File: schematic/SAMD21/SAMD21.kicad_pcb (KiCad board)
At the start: 4 copper layers, 100 x 100 mm, 54 parts, among them IC1 ATSAMD21G18A-AU, IC2 AZ1117IH-3.3TRG1, IC3 MCP2221-I_SL, J1 Barrel_Jack_Switch, J10 Conn_02x06_Odd_Even, J11 Conn_02x06_Odd_Even, J12 Conn_02x06_Odd_Even, J13 Conn_01x02, J14 Conn_02x05_Odd_Even, J15 Conn_01x08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

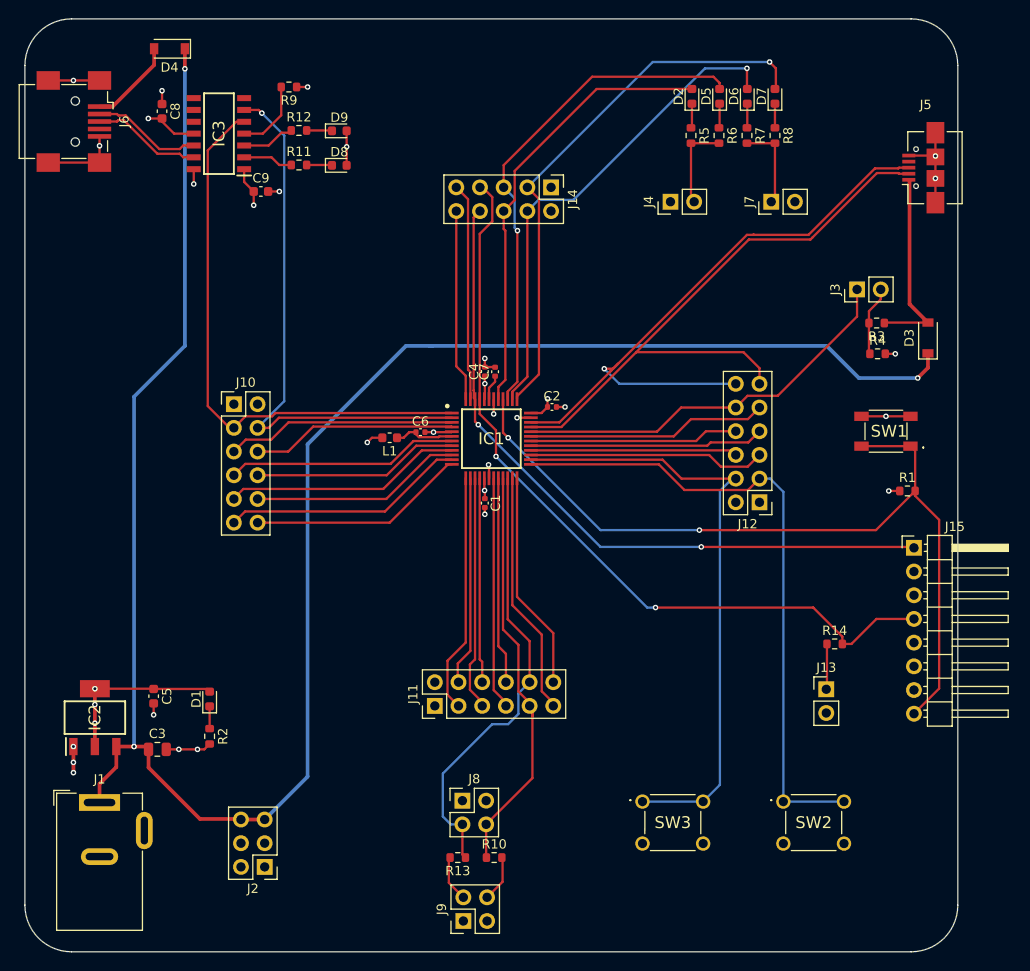
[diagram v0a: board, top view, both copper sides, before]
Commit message: Minor trace adjustments and some labels
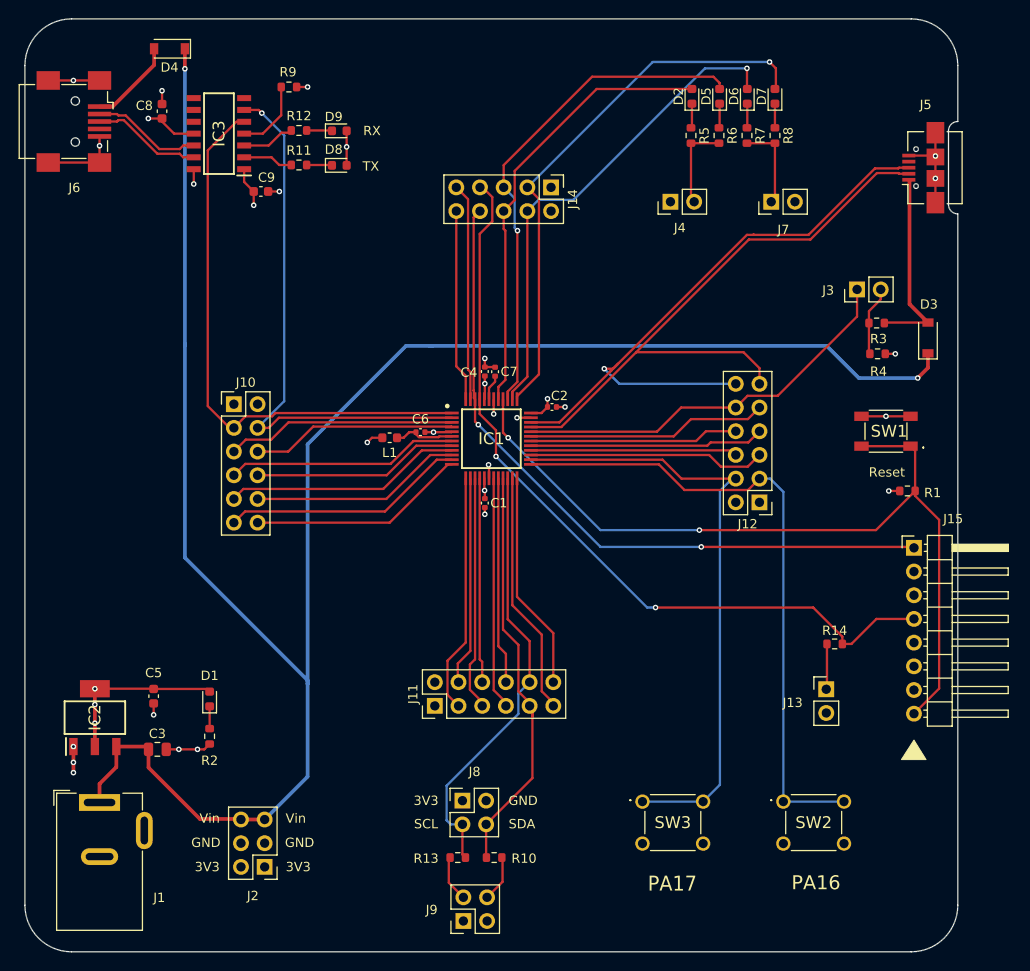
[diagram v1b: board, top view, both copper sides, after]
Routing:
- net VIN: track 220.9 -> 217.5 mm, vias 3 -> 2
- net SERCOM2_PAD1: track 48.2 -> 46.9 mm
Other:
- outline, holes or cut-outs redrawn
- board text added: "3V3"
- board text added: "GND"
- board text added: "JLCJLCJLCJLC"
- board text added: "Jumpers: J3 = USB Vbus Sense Enable J4, J7 = LED enable J9 = I2C pull-ups J13 = SWCLK pull-up"
- board text added: "PA16"
- board text added: "PA17"
- board text added: "QES 2021"
- board text added: "RX"
- board text added: "Reset"
- board text added: "SAMD21 Demo"
- board text added: "SCL"
- board text added: "SDA"
- board text added: "TX"
- board text added: "V1.0 ATSAMD21G18A"
- board text added: "Vin"

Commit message: Finished silkscreen
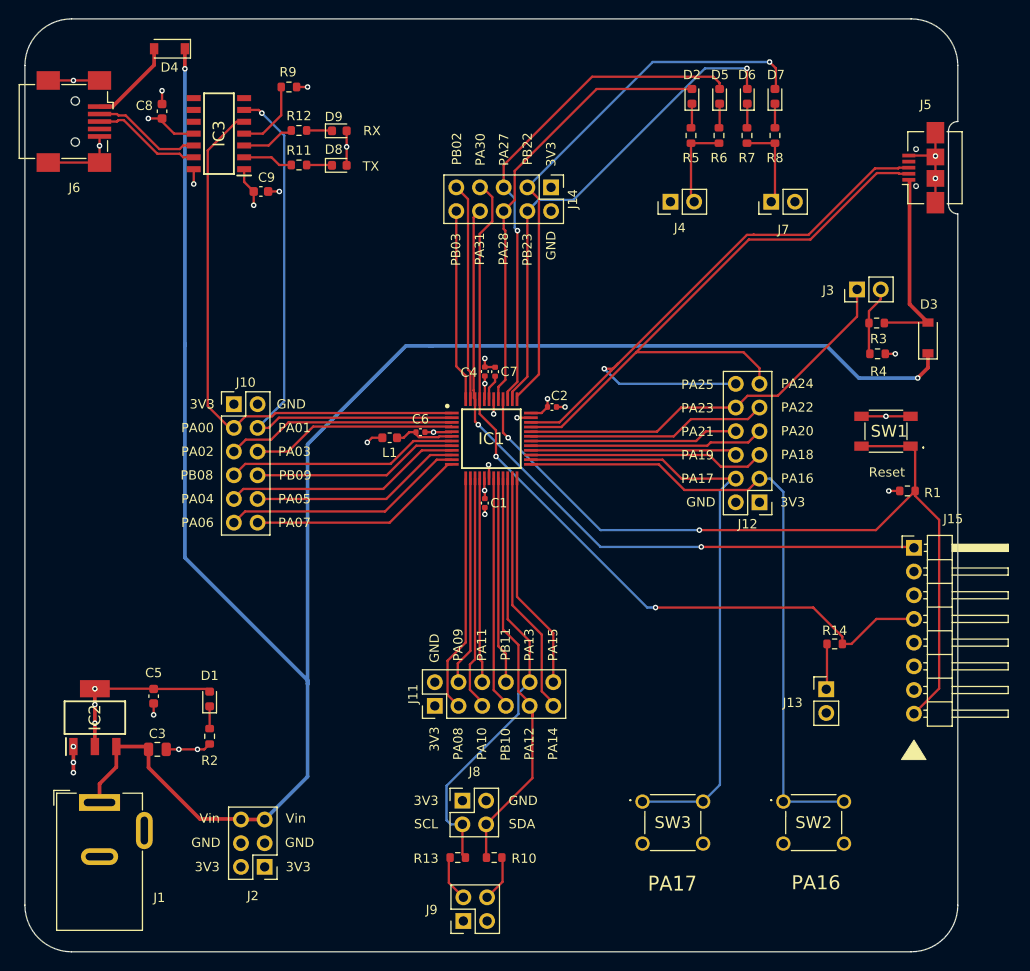
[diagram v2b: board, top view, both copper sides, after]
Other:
- board text added: "PA00"
- board text added: "PA01"
- board text added: "PA02"
- board text added: "PA03"
- board text added: "PA04"
- board text added: "PA05"
- board text added: "PA06"
- board text added: "PA07"
- board text added: "PA08"
- board text added: "PA09"
- board text added: "PA10"
- board text added: "PA11"
- board text added: "PA12"
- board text added: "PA13"
- board text added: "PA14"
- board text added: "PA15"
- board text added: "PA18"
- board text added: "PA19"
- board text added: "PA20"
- board text added: "PA21"
- board text added: "PA22"
- board text added: "PA23"
- board text added: "PA24"
- board text added: "PA25"
- board text added: "PA27"
- board text added: "PA28"
- board text added: "PA30"
- board text added: "PA31"
- board text added: "PB02"
- board text added: "PB03"
- board text added: "PB08"
- board text added: "PB09"
- board text added: "PB10"
- board text added: "PB11"
- board text added: "PB22"
- board text added: "PB23"

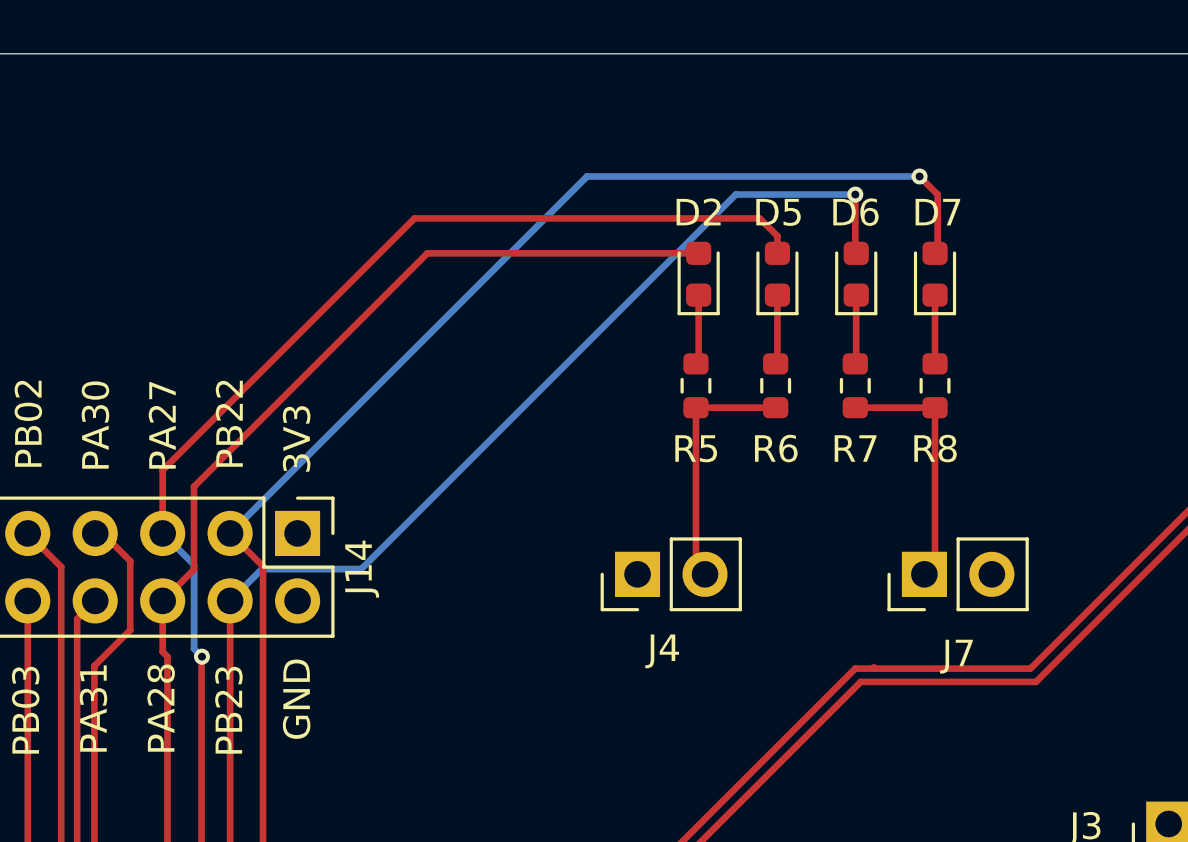
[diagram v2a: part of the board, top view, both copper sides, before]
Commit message: Changed LEDs to 0805
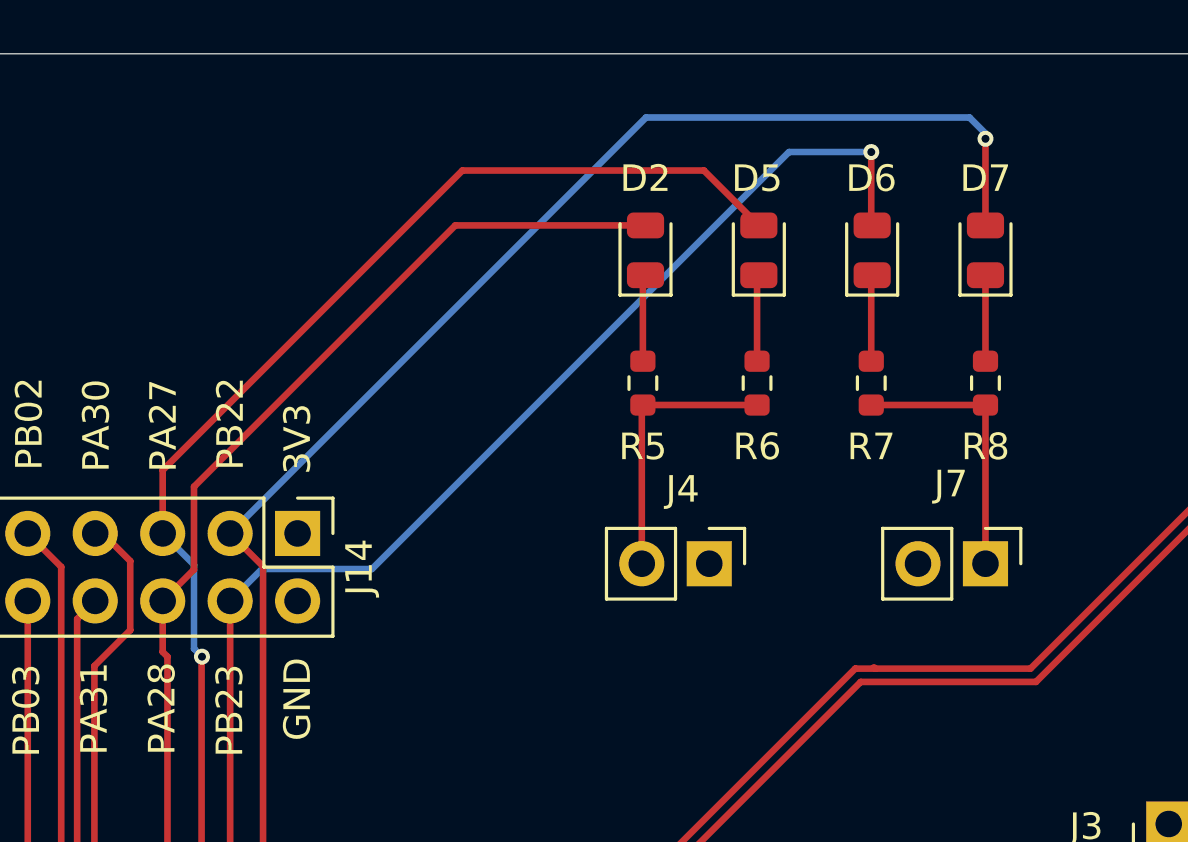
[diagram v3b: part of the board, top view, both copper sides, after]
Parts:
- D2, D5, D6, D7: footprint LED_SMD:LED_0603_1608Metric -> LED_SMD:LED_0805_2012Metric
- moved J4 2.73 mm to (136.9, 59.2), turned to 270 degrees
- moved J7 2.33 mm to (147.3, 59.2), turned to 270 degrees
- moved D2 2.19 mm to (134.5, 47.4)
- moved D7 2.10 mm to (147.3, 47.4)
- moved R5 2.00 mm to (134.4, 52.4)
- moved R8 1.90 mm to (147.3, 52.4)
- moved D5 1.14 mm to (138.8, 47.4)
- moved D6 1.08 mm to (143.0, 47.4)
- moved R6 0.71 mm to (138.7, 52.4)
- moved R7 0.61 mm to (143.0, 52.4)
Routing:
- net PB22: track 58.9 -> 62.8 mm
- net PB23: track 52.9 -> 54.7 mm
- net PA28: track 48.0 -> 46.4 mm
- net Net-(J4-Pad2): track 9.42 -> 10.3 mm
- net Net-(J7-Pad1): track 9.44 -> 10.3 mm
- net Net-(D7-Pad1): track 2.59 -> 3.24 mm
- net Net-(D6-Pad1): track 2.60 -> 3.25 mm
- net Net-(D2-Pad1): track 2.63 -> 3.28 mm
- net Net-(D5-Pad1): track 2.74 -> 3.27 mm

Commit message: minor fix
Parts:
- moved J15 0.32 mm to (160.6, 96.6)
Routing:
- net SERCOM2_PAD1: track 46.9 -> 45.0 mm
- net Net-(D3-Pad2): track 20.8 -> 22.4 mm
- net VCC3V3: vias 12 -> 11
- net GND: vias 22 -> 21

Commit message: Changed USB micro footprint
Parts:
- J5: footprint SamacSys_Parts:USB_Micro-B_Amphenol_10104110_Horizontal-With_pins -> Connector_USB:USB_Micro-B_Amphenol_10118194_Horizontal
- moved J1 0.45 mm to (73.0, 124.5)
- moved J5 0.05 mm to (161.2, 56.0)
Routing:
- net GND: vias 21 -> 19
